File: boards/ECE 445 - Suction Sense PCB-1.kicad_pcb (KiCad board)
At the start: 2 copper layers, 92.7 x 88.9 mm, 36 parts, among them J1 Paddle Sensor, J2 Motion Sensor, J3 Battery Connector, J4 Barrel_Jack, U1 ESP32-WROOM-32E, U2 TPS2120YFPR, U3 AP62150Z6, U4 MCP73831-2-OT

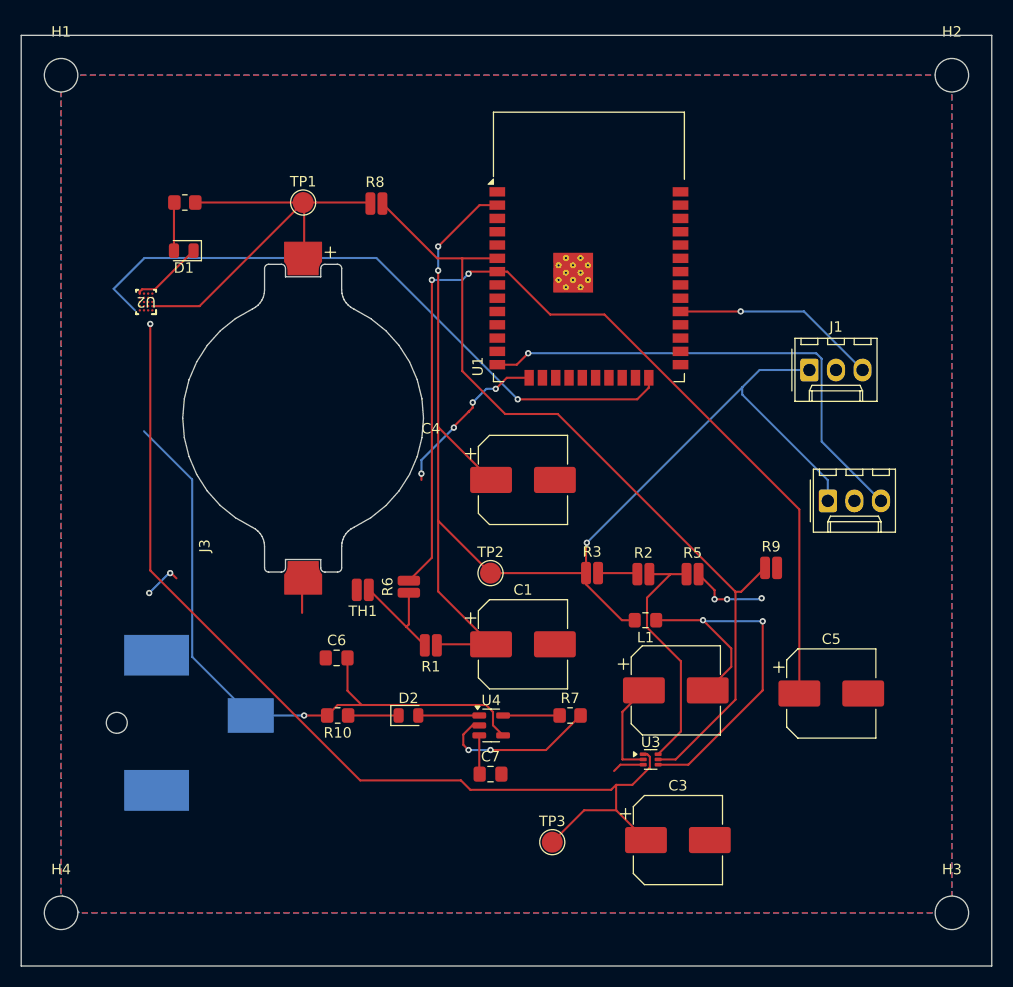
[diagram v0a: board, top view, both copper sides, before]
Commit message: routed with new footprint
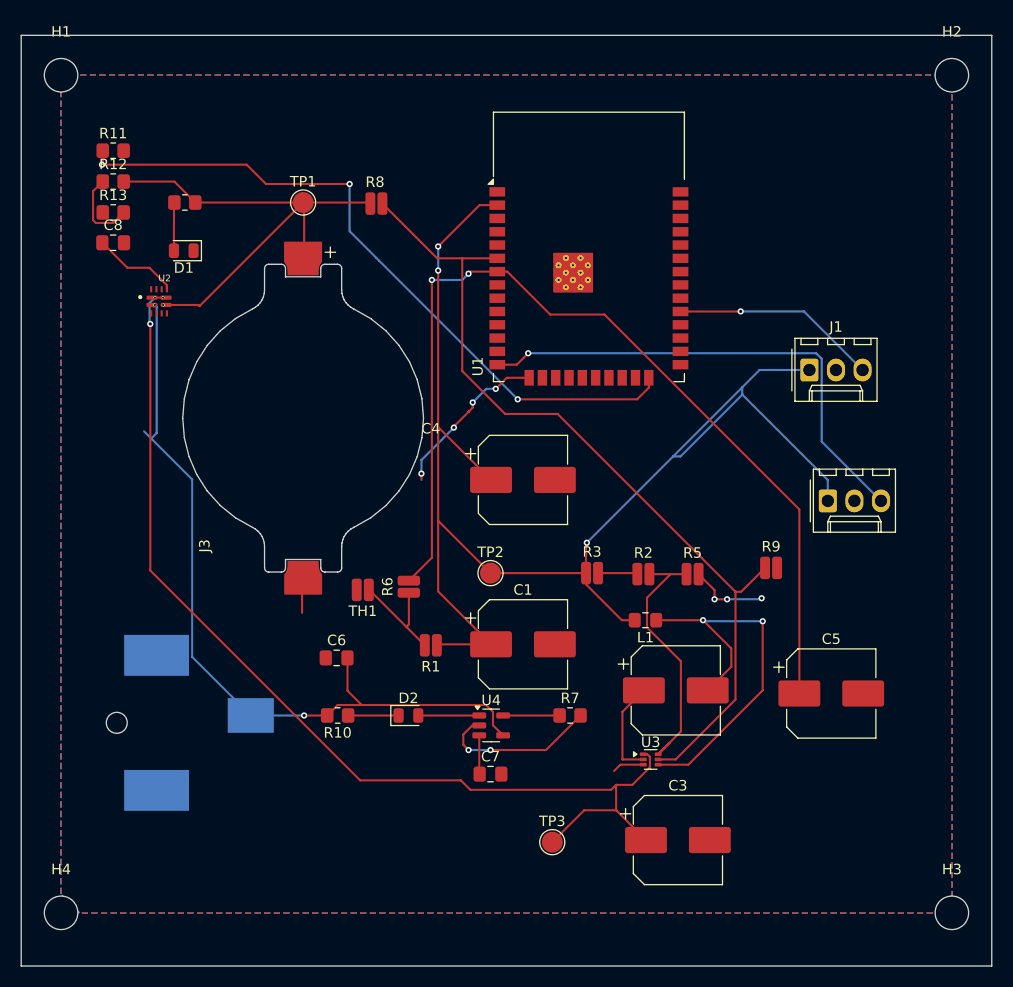
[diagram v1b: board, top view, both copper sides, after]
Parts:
- added C8: 1uF, Capacitor_SMD:C_0805_2012Metric_Pad1.18x1.45mm_HandSolder, F.Cu at (99.0, 69.3)
- added R11: 5k, Resistor_SMD:R_0805_2012Metric_Pad1.20x1.40mm_HandSolder, F.Cu at (99.0, 60.5)
- added R12: 20k, Resistor_SMD:R_0805_2012Metric_Pad1.20x1.40mm_HandSolder, F.Cu at (99.0, 63.5)
- added R13: 5k, Resistor_SMD:R_0805_2012Metric_Pad1.20x1.40mm_HandSolder, F.Cu at (99.0, 66.4)
- U2: value TPS2120YFPR -> TPS2121RUXR; footprint Library:YFP0020AAAA -> KiCadExtras:IC_TPS2121RUXR
- moved U2 1.24 mm to (103.3, 74.9), turned to 0 degrees
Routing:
- net +5VB: track 62.8 -> 76.6 mm
- net /3v3: track 128.3 -> 137.4 mm
- net Net-(U2-ST): track 0.00 -> 8.24 mm
- net Net-(R12-Pad1): track 0.00 -> 7.52 mm
- net GND: track 37.1 -> 30.2 mm
- net +3.7VA: track 41.1 -> 47.9 mm
- net /IO2: track 62.2 -> 66.9 mm, vias 1 -> 3
- net /BUCK_IN: track 96.4 -> 100.5 mm
- net (no net): track 3.59 -> 0.00 mm, vias 2 -> 0
- net Net-(D1-A): track 4.73 -> 6.99 mm
- net Net-(U3-FB): track 23.9 -> 25.5 mm

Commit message: adding new changes to pcb
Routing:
- net GND: track 30.2 -> 38.8 mm, vias 7 -> 9
- net (no net): track 0.00 -> 5.83 mm, vias 0 -> 2
- net /IO2: track 66.9 -> 66.1 mm, vias 3 -> 2
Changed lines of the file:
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@@
 			(drillshape 0)
 			(scaleselection 1)
-			(outputdirectory "")
+			(outputdirectory "./")
 		)
 	)
@@
 		(pad "1" smd roundrect
 			(at -0.7125 -0.5)
-			(size 0.675 0.35)
+			(size 0.675 0.3)
 			(layers "F.Cu" "F.Mask" "F.Paste")
 			(roundrect_rratio 0.25)
@@
 		(pad "2" smd roundrect
 			(at -0.7125 0)
-			(size 0.675 0.35)
+			(size 0.675 0.3)
 			(layers "F.Cu" "F.Mask" "F.Paste")
 			(roundrect_rratio 0.25)
@@
 		(pad "3" smd roundrect
 			(at -0.7125 0.5)
-			(size 0.675 0.35)
+			(size 0.675 0.3)
 			(layers "F.Cu" "F.Mask" "F.Paste")
 			(roundrect_rratio 0.25)
@@
 		(pad "4" smd roundrect
 			(at 0.7125 0.5)
-			(size 0.675 0.35)
+			(size 0.675 0.3)
 			(layers "F.Cu" "F.Mask" "F.Paste")
 			(roundrect_rratio 0.25)
@@
 		(pad "5" smd roundrect
 			(at 0.7125 0)
-			(size 0.675 0.35)
+			(size 0.675 0.3)
 			(layers "F.Cu" "F.Mask" "F.Paste")
 			(roundrect_rratio 0.25)
@@
 		(pad "6" smd roundrect
 			(at 0.7125 -0.5)
-			(size 0.675 0.35)
+			(size 0.675 0.3)
 			(layers "F.Cu" "F.Mask" "F.Paste")
 			(roundrect_rratio 0.25)
@@
 		(layer "Edge.Cuts")
 	)
+	(via
+		(at 98 74.2)
+		(size 0.6)
+		(drill 0.3)
+		(layers "F.Cu" "B.Cu")
+		(net 0)
+	)
+	(via
+		(at 102.3 70.5)
+		(size 0.6)
+		(drill 0.3)
+		(layers "F.Cu" "B.Cu")
+		(net 0)
+	)
+	(segment
+		(start 102.3 70.5)
+		(end 101.7 70.5)
+		(width 0.2)
+		(layer "B.Cu")
+		(net 0)
+	)
+	(segment
+		(start 101.7 70.5)
+		(end 98 74.2)
+		(width 0.2)
+		(layer "B.Cu")
+		(net 0)
+	)
 	(segment
 		(start 135 100.9)
@@
 	)
 	(segment
+		(start 101.613 73.787)
+		(end 101.6 73.8)
+		(width 0.2)
+		(layer "F.Cu")
+		(net 2)
+	)
+	(segment
 		(start 128.4 91.4)
 		(end 128.4 92)
@@
 	)
 	(segment
+		(start 101.413 76.087)
+		(end 101.4 76.1)
+		(width 0.2)
+		(layer "F.Cu")
+		(net 2)
+	)
+	(segment
 		(start 132.95 85.45)
 		(end 132.9 85.5)
@@
 	)
 	(segment
+		(start 102.588 76.087)
+		(end 104.088 76.087)
+		(width 0.2)
+		(layer "F.Cu")
+		(net 2)
+	)
+	(segment
+		(start 102.588 73.787)
+		(end 102.1 73.787)
+		(width 0.2)
+		(layer "F.Cu")
+		(net 2)
+	)
+	(segment
+		(start 102.1 73.787)
+		(end 101.613 73.787)
+		(width 0.2)
+		(layer "F.Cu")
+		(net 2)
+	)
+	(segment
 		(start 131.5 86.9)
 		(end 131.5 87)
@@
 	)
 	(segment
+		(start 149.588 119.2)
+		(end 149.188 119.6)
+		(width 0.2)
+		(layer "F.Cu")
+		(net 2)
+	)
+	(segment
 		(start 133.3 84.6)
 		(end 133.3 85.1)
@@
 	)
 	(segment
-		(start 147.4 119.2)
-		(end 146.8 119.8)
+		(start 156.4 103.4)
+		(end 157.6 103.4)
 		(width 0.2)
 		(layer "F.Cu")
@@
 	)
 	(segment
-		(start 149.588 119.2)
-		(end 147.4 119.2)
+		(start 154.875 101)
+		(end 156.4 102.525)
 		(width 0.2)
 		(layer "F.Cu")
@@
 	)
 	(segment
-		(start 156.4 103.4)
-		(end 157.6 103.4)
+		(start 133.3 85.1)
+		(end 132.95 85.45)
 		(width 0.2)
 		(layer "F.Cu")
@@
 	)
 	(segment
-		(start 154.875 101)
-		(end 156.4 102.525)
+		(start 102.588 76.087)
+		(end 101.413 76.087)
 		(width 0.2)
 		(layer "F.Cu")
@@
 	)
 	(segment
-		(start 133.3 85.1)
-		(end 132.95 85.45)
+		(start 138.69 82.241)
+		(end 136.559 82.241)
 		(width 0.2)
 		(layer "F.Cu")
@@
 	)
 	(segment
-		(start 138.69 82.241)
-		(end 136.559 82.241)
+		(start 149.188 119.6)
+		(end 147 119.6)
+		(width 0.2)
+		(layer "F.Cu")
+		(net 2)
+	)
+	(segment
+		(start 147 119.6)
+		(end 146.8 119.8)
 		(width 0.2)
 		(layer "F.Cu")
@@
 	)
 	(via
+		(at 114 66.6)
+		(size 0.6)
+		(drill 0.3)
+		(layers "F.Cu" "B.Cu")
+		(free yes)
+		(net 2)
+	)
+	(via
 		(at 160.9 103.3)
 		(size 0.6)
@@
 		(net 2)
 	)
+	(via
+		(at 115.1 62.1)
+		(size 0.6)
+		(drill 0.3)
+		(layers "F.Cu" "B.Cu")
+		(net 2)
+	)
+	(segment
+		(start 114 66.6)
+		(end 114 63.2)
+		(width 0.2)
+		(layer "B.Cu")
+		(net 2)
+	)
 	(segment
 		(start 128.4 90.1)
@@
 	)
 	(segment
+		(start 114 63.2)
+		(end 115.1 62.1)
+		(width 0.2)
+		(layer "B.Cu")
+		(net 2)
+	)
+	(segment
 		(start 160.8 103.4)
 		(end 160.9 103.3)
@@
 	(segment
 		(start 111.709 61.8858)
-		(end 97.8835 61.8858)
+		(end 99.9 61.8858)
 		(width 0.2)
 		(layer "F.Cu")
@@
 	)
 	(segment
-		(start 97.9575 61.8118)
-		(end 97.8835 61.8858)
+		(start 99.2943 61.8858)
+		(end 99.9 61.8858)
 		(width 0.2)
 		(layer "F.Cu")
@@
 	(segment
 		(start 97.9575 60.549)
-		(end 97.9575 61.8118)
+		(end 99.2943 61.8858)
 		(width 0.2)
 		(layer "F.Cu")
@@
 		(size 0.6)
 		(drill 0.3)
-		(layers "F.Cu" "B.Cu")
-		(net 37)
-	)
-	(via
-		(at 97.8835 61.8858)
-		(size 0.6)
-		(drill 0.3)

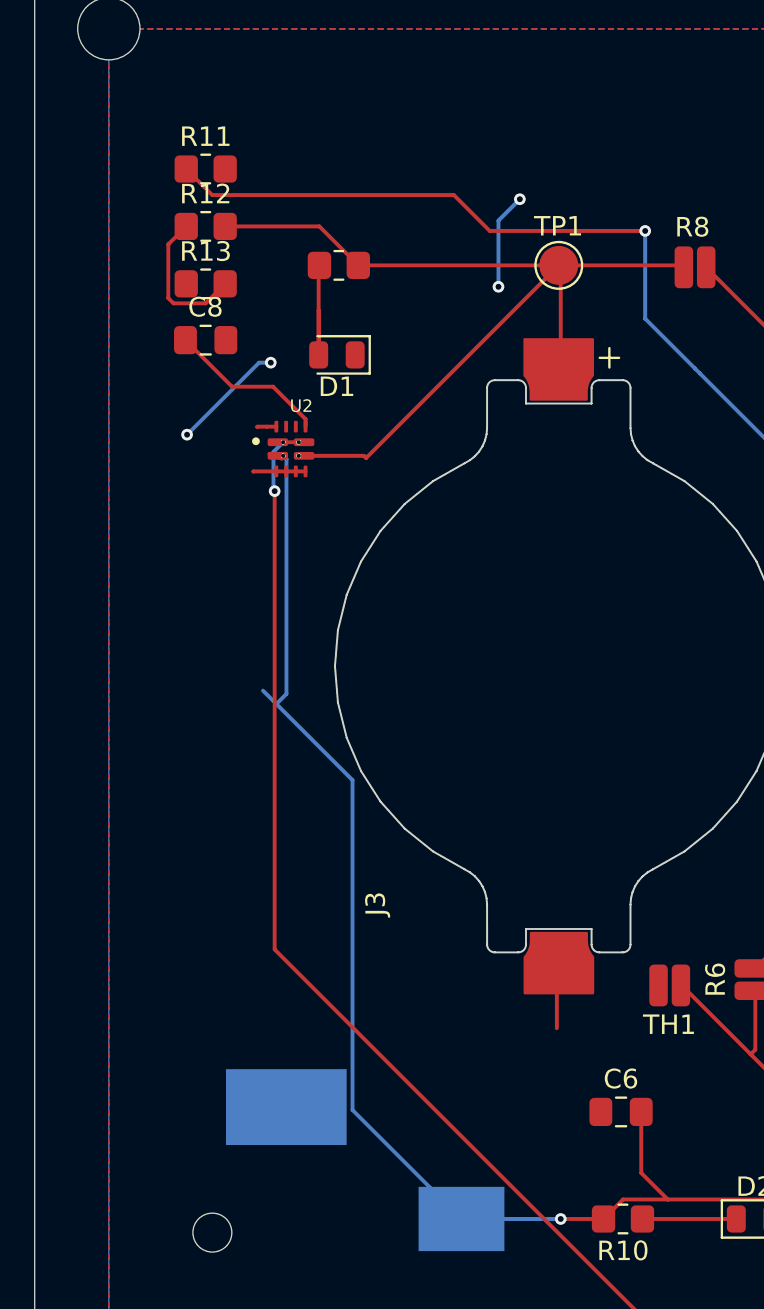
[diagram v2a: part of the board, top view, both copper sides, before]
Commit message: added boost converter
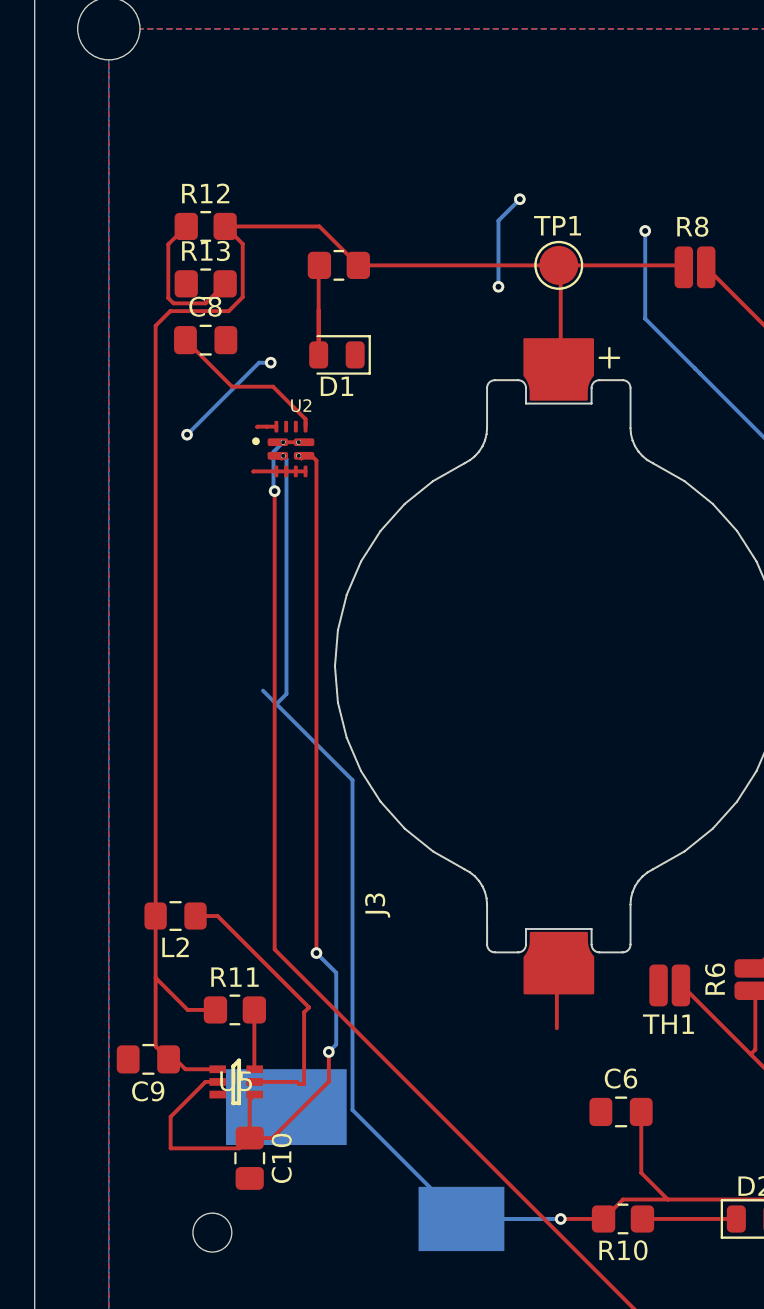
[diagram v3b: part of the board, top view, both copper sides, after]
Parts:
- added C10: 40uF, Capacitor_SMD:C_0805_2012Metric_Pad1.18x1.45mm_HandSolder, F.Cu at (101.2, 111.4)
- added C9: 10uF, Capacitor_SMD:C_0805_2012Metric_Pad1.18x1.45mm_HandSolder, F.Cu at (96.0, 106.3)
- added L2: 3.3uH, Inductor_SMD:L_0805_2012Metric_Pad1.15x1.40mm_HandSolder, F.Cu at (97.4, 98.9)
- added U5: TPS61222DCKR, KiCadExtras:DCK0006A, F.Cu at (100.5, 107.5)
- R11: value 5k -> 100K
- moved R11 43.2 mm to (100.5, 103.8)
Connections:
- D1 pad 2: Net-(D1-A) -> GND
- R11 pad 1: /IO2 -> +3.7VA
- R11 pad 2: GND -> Net-(U5-EN)
- R4 pad 1: Net-(D1-A) -> GND
- U2 pad 7: +3.7VA -> /5vA
- U2 pad 7_1: +3.7VA -> /5vA
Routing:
- net /5vA: track 0.00 -> 50.3 mm, vias 0 -> 2
- net +3.7VA: track 47.9 -> 84.0 mm
- net /IO2: track 66.1 -> 41.2 mm
- net Net-(U5-L): track 0.00 -> 14.4 mm
- net Net-(D1-A): track 6.99 -> 0.00 mm
- net GND: track 38.8 -> 45.8 mm
- net Net-(U5-EN): track 0.00 -> 3.05 mm

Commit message: changed schematic and baord
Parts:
- added C11: 22uf, Capacitor_SMD:C_0805_2012Metric_Pad1.18x1.45mm_HandSolder, F.Cu at (125.9, 66.2)
- added C12: 0.1uf, Capacitor_SMD:C_0805_2012Metric_Pad1.18x1.45mm_HandSolder, F.Cu at (130.0, 66.2)
- added C13: 1uf, Capacitor_SMD:C_0805_2012Metric_Pad1.18x1.45mm_HandSolder, F.Cu at (133.3, 68.6)
- added J5: Conn_01x06_Pin, Connector_Molex:Molex_KK-396_A-41791-0006_1x06_P3.96mm_Vertical, F.Cu at (113.4, 128.4)
- added R14: R, Resistor_SMD:R_0805_2012Metric_Pad1.20x1.40mm_HandSolder, F.Cu at (150.6, 89.8)
- moved R9 45.9 mm to (125.0, 73.0), turned to -90 degrees
- moved J2 24.3 mm to (167.4, 69.7), turned to 180 degrees
- moved R8 3.38 mm to (121.8, 68.1)
- moved J1 0.19 mm to (165.4, 81.7)
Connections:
- R8 pad 2: /EN -> /IO34
- R9 pad 1: /EN -> /IO34
- U1 pad 25: unconnected-(U1-IO0-Pad25) -> Net-(J5-Pin_4)
- U1 pad 3: unconnected-(U1-EN-Pad3) -> Net-(J5-Pin_5)
- U1 pad 34: unconnected-(U1-RXD0/IO3-Pad34) -> Net-(J5-Pin_2)
- U1 pad 35: unconnected-(U1-TXD0/IO1-Pad35) -> Net-(J5-Pin_3)
- U1 pad 6: /EN -> /IO34
- U3 pad 5: /EN -> /BUCK_IN
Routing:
- net Net-(J5-Pin_5): track 0.00 -> 181.2 mm, vias 0 -> 2
- net Net-(J5-Pin_2): track 0.00 -> 145.1 mm
- net Net-(J5-Pin_4): track 0.00 -> 142.9 mm
- net Net-(J5-Pin_3): track 0.00 -> 141.2 mm, vias 0 -> 2
- net /BUCK_IN: track 100.5 -> 184.9 mm, vias 1 -> 3
- net /EN: track 82.6 -> 0.00 mm
- net /IO12: track 47.6 -> 101.3 mm
- net /3v3: track 137.4 -> 160.8 mm
- net /IO34: track 0.00 -> 16.8 mm
- net GND: track 45.8 -> 55.9 mm
- net +3.7VA: track 84.0 -> 77.5 mm

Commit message: edit schematic
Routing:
- net /IO2: track 41.2 -> 13.9 mm, vias 2 -> 1
- net /3v3: track 160.8 -> 147.3 mm
- net (no net): track 6.27 -> 0.00 mm, vias 2 -> 0
- net +3.7VA: track 77.5 -> 82.7 mm
- net /BUCK_IN: track 184.9 -> 188.7 mm
- net /IO12: track 101.3 -> 97.8 mm, vias 1 -> 0
- net GND: track 55.9 -> 54.7 mm
- net +5VB: track 76.6 -> 76.3 mm, vias 1 -> 2

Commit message: new baord
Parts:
- U3: footprint Package_TO_SOT_SMD:SOT-563 -> Package_TO_SOT_SMD:TSOT-23-6_HandSoldering
- moved U3 13.5 mm to (162.9, 123.5), turned to -90 degrees
- moved C3 3.98 mm to (152.7, 122.4), turned to 180 degrees
- moved R2 0.29 mm to (149.6, 100.7)
- moved L1 0.12 mm to (149.8, 105.3)
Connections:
- U5 pad 6: Net-(U5-EN) -> +3.7VA
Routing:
- net Net-(U3-FB): track 25.5 -> 50.6 mm, vias 0 -> 2
- net Net-(U3-SW): track 9.44 -> 25.7 mm, vias 0 -> 2
- net /IO12: track 97.8 -> 113.9 mm
- net /BUCK_IN: track 188.7 -> 200.5 mm, vias 3 -> 2
- net GND: track 54.7 -> 48.2 mm
- net Net-(U3-BST): track 38.5 -> 36.3 mm

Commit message: better footprint for boost
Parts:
- removed R11: 100K, Resistor_SMD:R_0805_2012Metric_Pad1.20x1.40mm_HandSolder
- C10: value 40uF -> 10uf
- C9: value 10uF -> 44uf
- L1: footprint Inductor_SMD:L_0805_2012Metric_Pad1.15x1.40mm_HandSolder -> Inductor_SMD:L_Changjiang_FTC201655S
- L2: value 3.3uH -> L; footprint Inductor_SMD:L_0805_2012Metric_Pad1.15x1.40mm_HandSolder -> Inductor_SMD:L_Changjiang_FTC201655S
- U5: value TPS61222DCKR -> TPS613222ADBVR; footprint KiCadExtras:DCK0006A -> KiCadExtras:SOT95P280X145-5N
- moved C10 15.1 mm to (96.8, 96.9), turned to 180 degrees
- moved C9 7.80 mm to (102.2, 111.0), turned to -90 degrees
- moved U5 2.64 mm to (100.8, 104.8)
- moved L2 2.01 mm to (98.0, 100.8), turned to -90 degrees
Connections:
- C10 pad 1: /5vA -> +3.7VA
- C9 pad 1: +3.7VA -> /5vA
- L2 pad 1: Net-(U5-L) -> +3.7VA
- L2 pad 2: +3.7VA -> Net-(U5-SW)
- U5 pad 1: +3.7VA -> Net-(U5-SW)
- U5 pad 2: /5vA -> GND
- U5 pad 3: GND -> (no net)
- U5 pad 5: Net-(U5-L) -> (no net)
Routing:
- net /5vA: track 50.3 -> 5.36 mm, vias 2 -> 0
- net +3.7VA: track 82.7 -> 101.9 mm, vias 0 -> 4
- net Net-(U5-L): track 14.4 -> 0.00 mm
- net Net-(U5-EN): track 3.05 -> 0.00 mm
- net Net-(U5-SW): track 0.00 -> 3.03 mm
